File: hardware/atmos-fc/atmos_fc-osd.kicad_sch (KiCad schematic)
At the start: 12 parts, among them U4 MAX7456, Y2 27MHz

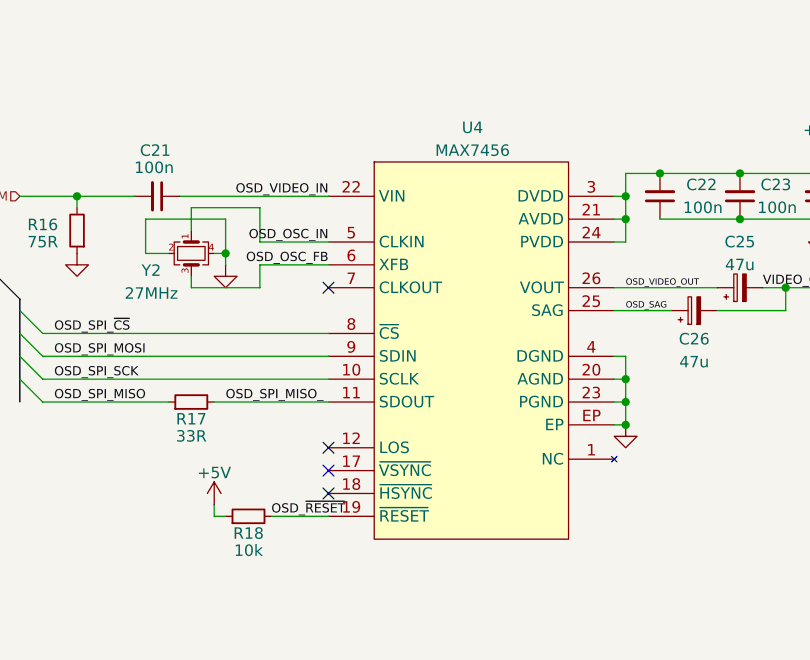
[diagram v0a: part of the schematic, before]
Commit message: Add soldering pads for ESC
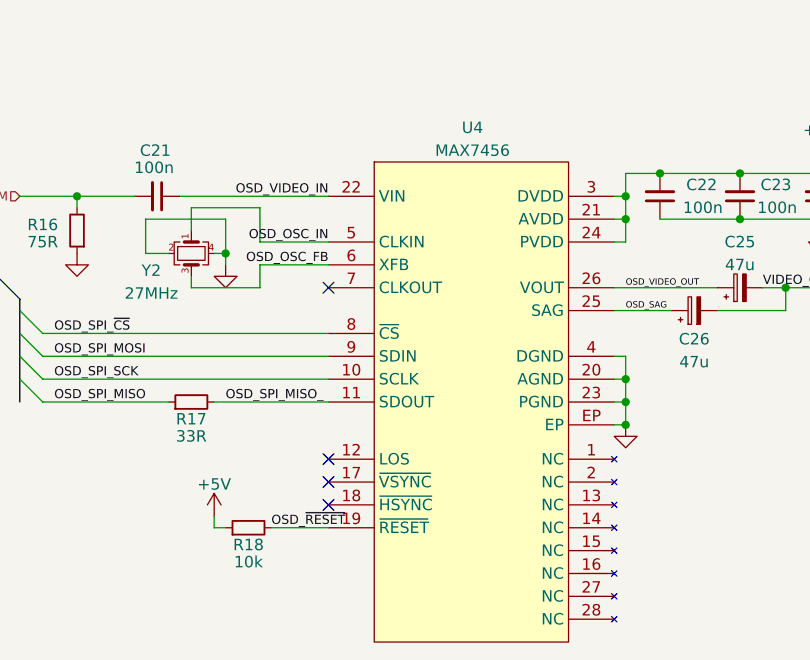
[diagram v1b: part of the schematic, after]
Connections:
- now unconnected: U4.1 (NC), U4.13 (NC), U4.14 (NC), U4.15 (NC), U4.16 (NC), U4.2 (NC), U4.27 (NC), U4.28 (NC)
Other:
- moved on the sheet: R18
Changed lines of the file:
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@@
 	)
 	(no_connect
-		(at 132.08 114.3)
+		(at 132.08 115.57)
 	)
 	(no_connect
-		(at 132.08 119.38)
+		(at 132.08 120.65)
 	)
 	(no_connect
-		(at 132.08 116.84)
+		(at 132.08 118.11)
 	)
 	(no_connect
@@
 	(wire
 		(pts
-			(xy 125.73 121.92) (xy 132.08 121.92)
+			(xy 125.73 123.19) (xy 132.08 123.19)
 		)
 		(stroke
@@
 	(wire
 		(pts
-			(xy 120.65 121.92) (xy 119.38 121.92)
+			(xy 120.65 123.19) (xy 119.38 123.19)
 		)
 		(stroke
@@
 	(wire
 		(pts
-			(xy 119.38 121.92) (xy 119.38 120.65)
+			(xy 119.38 123.19) (xy 119.38 121.92)
 		)
 		(stroke
@@
 	)
 	(label "OSD_~{RESET}"
-		(at 125.73 121.92 0)
+		(at 125.73 123.19 0)
 		(fields_autoplaced yes)
 		(effects
@@
 		(lib_name "+5V_1")
 		(lib_id "power:+5V")
-		(at 119.38 120.65 0)
+		(at 119.38 121.92 0)
 		(unit 1)
 		(exclude_from_sim no)
@@
 		(dnp no)
 		(property "Reference" "#PWR038"
-			(at 119.38 124.46 0)
+			(at 119.38 125.73 0)
 			(effects
 				(font
@@
 		)
 		(property "Value" "+5V"
-			(at 119.38 117.094 0)
+			(at 119.38 118.364 0)
 			(effects
 				(font
@@
 		)
 		(property "Footprint" ""
-			(at 119.38 120.65 0)
+			(at 119.38 121.92 0)
 			(effects
 				(font
@@
 		)
 		(property "Datasheet" ""
-			(at 119.38 120.65 0)
+			(at 119.38 121.92 0)
 			(effects
 				(font
@@
 		)
 		(property "Description" "Power symbol creates a global label with name \"+5V\""
-			(at 119.38 120.65 0)
+			(at 119.38 121.92 0)
 			(effects
 				(font
@@
 	(symbol
 		(lib_id "Device:R_Small")
-		(at 123.19 121.92 90)
+		(at 123.19 123.19 90)
 		(unit 1)
 		(exclude_from_sim no)
@@
 		(dnp no)
 		(property "Reference" "R18"
-			(at 123.19 123.825 90)
+			(at 123.19 125.095 90)
 			(effects
 				(font
@@
 		)
 		(property "Value" "10k"
-			(at 123.19 125.73 90)
+			(at 123.19 127 90)
 			(effects
 				(font
@@
 		)
 		(property "Footprint" "Resistor_SMD:R_0402_1005Metric"
-			(at 123.19 121.92 0)
+			(at 123.19 123.19 0)
 			(effects
 				(font
@@
 		)
 		(property "Datasheet" "~"
-			(at 123.19 121.92 0)
+			(at 123.19 123.19 0)
 			(effects
 				(font
@@
 		)
 		(property "Description" "Thick Film Resistors - SMD 1/16watt 10Kohms 1% Commercial Use"
-			(at 123.19 121.92 0)
+			(at 123.19 123.19 0)
 			(effects
 				(font
@@
 		)
 		(property "Manufacturer" "Vishay / Dale"
-			(at 123.19 121.92 0)
+			(at 123.19 123.19 0)
 			(effects
 				(font
@@
 		)
 		(property "Mfr Part Number" "CRCW040210K0FKEDC"
-			(at 123.19 121.92 0)
-			(effects
-				(font
+			(at 123.19 123.19 0)
+			(effects
+				(font
